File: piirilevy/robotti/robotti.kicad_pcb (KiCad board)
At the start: 2 copper layers, 86.7 x 68.6 mm, 63 parts, among them J1 VL53L1X, J2 VL53L1X, J3 XT30, J4 ST-LINK_V2, J5 UART, J6 Nema14, J7 Nema14, Q1 ALS-PT19-315C, SW1 SW_SPST, U1 ICM-42605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

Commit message: PCB V2.0
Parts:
- removed C1: 10nF, Capacitor_SMD:C_0805_2012Metric
- removed C2: 0.1uF, Capacitor_SMD:C_0805_2012Metric
- removed C3: 2.2uF, Capacitor_SMD:C_0805_2012Metric
- added REF**: MountingHole_3.2mm_M3, MountingHole:MountingHole_3.2mm_M3, F.Cu at (94.2, 111.1)
- added REF**: MountingHole_3.2mm_M3, MountingHole:MountingHole_3.2mm_M3, F.Cu at (174.6, 111.1)
- added REF**: MountingHole_3.2mm_M3, MountingHole:MountingHole_3.2mm_M3, F.Cu at (174.6, 48.9)
- added REF**: MountingHole_3.2mm_M3, MountingHole:MountingHole_3.2mm_M3, F.Cu at (94.2, 48.9)
- U1: value ICM-42605 -> SEN0373; footprint Package_LGA:LGA-14_3x2.5mm_P0.5mm_LayoutBorder3x4y -> robotti:PinHeader_1x07_PinHeader_SEN0373
- moved C6 49.7 mm to (96.6, 60.4)
- moved R1 19.4 mm to (120.4, 63.4), turned to 270 degrees
- moved R2 16.0 mm to (118.2, 63.4), turned to 270 degrees
- moved D3 14.7 mm to (102.3, 73.2)
- moved D2 13.3 mm to (102.3, 75.4)
- moved R3 12.9 mm to (116.1, 63.4), turned to 270 degrees
- moved D1 12.0 mm to (102.3, 77.7)
- moved C11 10.9 mm to (118.9, 73.5)
- moved U1 9.15 mm to (110.1, 67.8), turned to 270 degrees
- moved U3 8.71 mm to (115.1, 72.8), turned to 90 degrees
- moved R13 6.48 mm to (142.0, 94.6)
- moved C13 6.33 mm to (112.1, 75.8), turned to 180 degrees
- moved R12 5.59 mm to (142.0, 97.5)
- moved FB1 5.45 mm to (142.8, 77.5), turned to 0 degrees
- moved C27 4.90 mm to (166.6, 108.2), turned to 270 degrees
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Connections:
- net Net-(C8-Pad2) renamed /VDDA
- C11 pad 1: Net-(C11-Pad1) -> /PC13
- J1 pad 4: /PB7 -> /PB11
- J1 pad 5: /PB6 -> /PB10
- J2 pad 4: /PB11 -> /PB14
- J2 pad 5: /PB10 -> /PB15
- J5 pad 1: /PA2 -> /PA11
- J5 pad 2: /PA3 -> /PC7
- JP1 pad 1: /PC1 -> /PB12
- JP1 pad 2: /PC2 -> /PC6
- JP1 pad 8: /PC3 -> /PC8
- JP2 pad 8: /PA9 -> /PB2
- Q1 pad 2: Net-(Q1-Pad2) -> /PC14
- R12 pad 2: /PC0 -> /PC1
- R13 pad 2: /PC0 -> /PC1
- R3 pad 1: Net-(R3-Pad1) -> /PA15
- R6 pad 1: Net-(Q1-Pad2) -> /PC14
- U1 pad 1: GND -> VDD
- U1 pad 2: Net-(U1-Pad2) -> GND
- U1 pad 3: Net-(U1-Pad3) -> /PB6
- U1 pad 4: /PC8 -> /PB7
- U1 pad 5: VDD -> Net-(U1-Pad5)
- U1 pad 6: GND -> /PB4
- U1 pad 7: GND -> /PC12
- U2 pad 14: Net-(Q1-Pad2) -> Net-(U2-Pad14)
- U2 pad 15: Net-(C11-Pad1) -> /PA1
- U2 pad 2: Net-(R3-Pad1) -> /PC13
- U2 pad 28: Net-(U2-Pad28) -> /PB2
- U2 pad 3: Net-(U2-Pad3) -> /PC14
- U2 pad 37: Net-(U2-Pad37) -> /PC6
- U2 pad 44: Net-(U2-Pad44) -> /PA11
- U2 pad 50: Net-(U2-Pad50) -> /PA15
- U2 pad 51: Net-(U2-Pad51) -> Net-(R2-Pad1)
- U2 pad 53: Net-(R2-Pad1) -> /PC12
- U2 pad 56: Net-(U2-Pad56) -> /PB4
- U2 pad 57: Net-(U2-Pad57) -> /PB5
- U3 pad 2: Net-(C11-Pad1) -> /PC13
- U4 pad 13: /PB14 -> /PC2
- U4 pad 14: /PB15 -> /PC3
- U4 pad 15: /PB12 -> /PB9
- U4 pad 6: /PB9 -> /PB5
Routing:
- net /PA3: track 62.1 -> 0.00 mm, vias 2 -> 0
- net /PA2: track 57.1 -> 0.00 mm, vias 1 -> 0
- net Net-(C11-Pad1): track 53.6 -> 0.00 mm, vias 2 -> 0
- net /PA9: track 52.0 -> 0.00 mm, vias 1 -> 0
- net /PB2: track 0.00 -> 44.4 mm, vias 0 -> 1
- net /PB5: track 0.00 -> 39.9 mm, vias 0 -> 2
- net /PA11: track 0.00 -> 35.6 mm, vias 0 -> 1
- net /PC12: track 0.00 -> 34.3 mm
- net /PC6: track 0.00 -> 33.9 mm, vias 0 -> 1
- net Net-(R3-Pad1): track 33.4 -> 0.00 mm
- net NRST: track 113.0 -> 81.4 mm, vias 3 -> 2
- net /PB4: track 0.00 -> 30.6 mm
- net /PA8: track 29.8 -> 0.00 mm, vias 2 -> 0
- net /PB15: track 40.6 -> 11.7 mm, vias 2 -> 0
- net Net-(Q1-Pad2): track 28.3 -> 0.00 mm, vias 2 -> 0
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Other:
- net class Default: clearance 0.1 -> 0.2; via_drill 0.4 -> 0.5
- net class GND added: clearance 0.2, trace_width 0.25, via_dia 0.8, via_drill 0.5
- net class VCC: clearance 0.2 -> 0.3; via_dia 1 -> 1.2
- rule trace_clearance: 0.1 -> 0.2
- rule trace_min: 0.2 -> 0.25
- rule via_min_drill: 0.3 -> 0.5
- rule via_min_size: 0.4 -> 0.8
- board text added: "GND"
- board text added: "LED1"
- board text added: "NRST"
- board text added: "RESET"
- board text added: "RX"
- board text added: "SWCLK"
- board text added: "SWDIO"
- board text added: "SWO"
- board text added: "TX"
- board text added: "VDD"

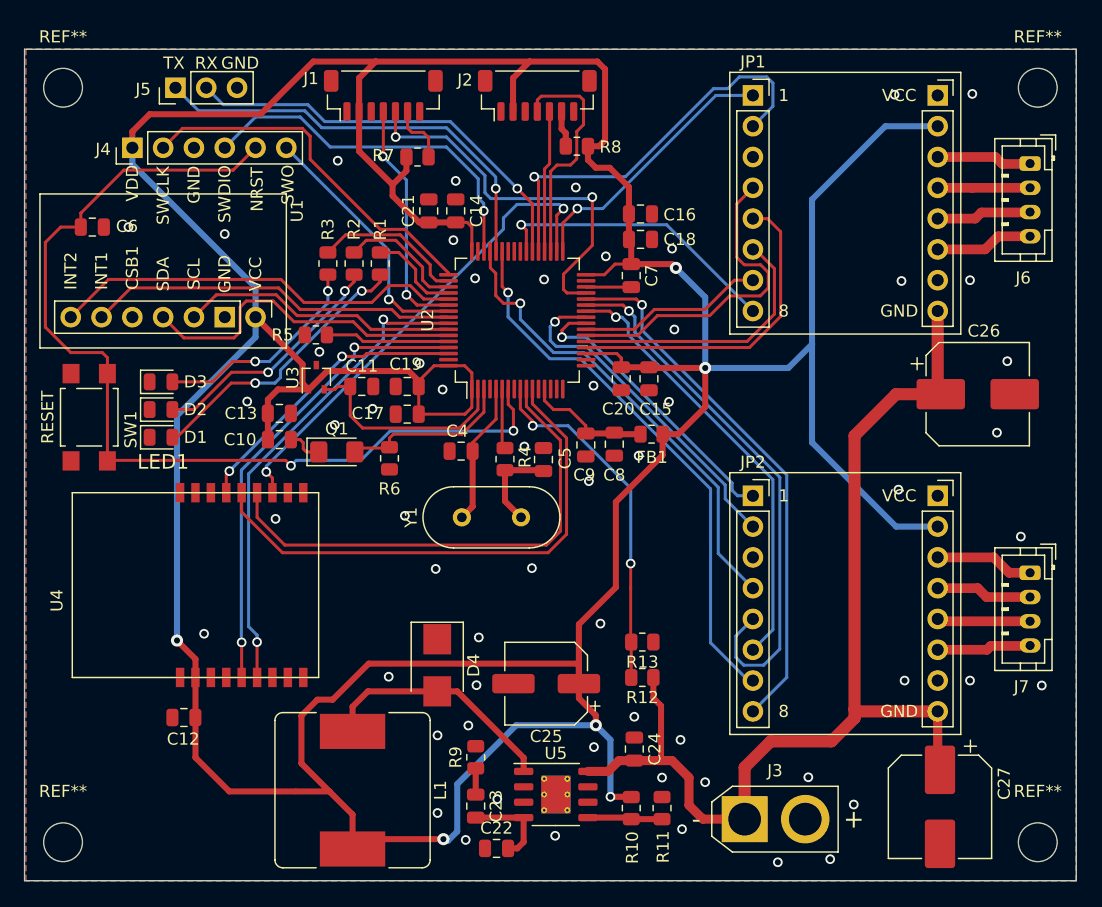
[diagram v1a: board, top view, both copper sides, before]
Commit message: Generoitu Platformio IO projekti CubeMX conffista
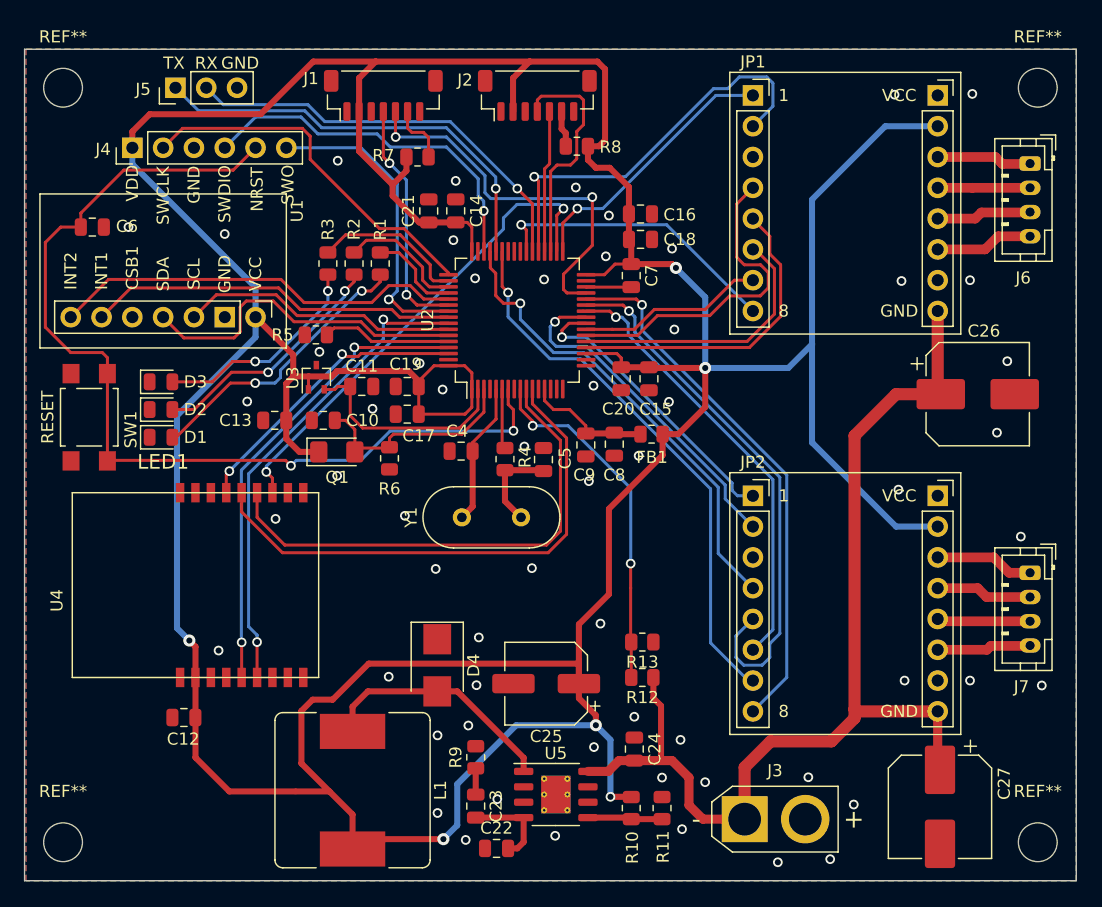
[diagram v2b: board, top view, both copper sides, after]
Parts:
- moved C10 3.95 mm to (115.7, 76.3)
- moved C13 0.69 mm to (111.7, 76.3), turned to 0 degrees
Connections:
- C10 pad 1: Net-(C10-Pad1) -> /PC14
- C10 pad 2: VDD -> GND
- Q1 pad 1: Net-(C10-Pad1) -> VDD
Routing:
- net /PB3: track 21.2 -> 25.4 mm
- net /PC14: track 14.4 -> 18.2 mm
- net Net-(C10-Pad1): track 3.01 -> 0.00 mm
- net VDD: track 394.9 -> 396.8 mm
- net GND: vias 58 -> 59
